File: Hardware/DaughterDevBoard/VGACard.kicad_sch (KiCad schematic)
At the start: 42 parts, among them J13 BANKA, J14 BANKB, J15 BANKD, J16 BANKC, J17 VGA_OUT, J19 BANK_A, J20 BANK_C, J21 BANK_B, J22 BANK_D, J8 PROG, Q1 2N2222A, U3 SN74LVC2T45QDCURQ1, U4 SN74LVC2T45QDCURQ1, U5 NE555P, U6 SN74LVC8T245DBQR, U7 SN74LVC8T245DBQR, U8 SN74LVC8T245DBQR, U9 SN74LVC1T45DCK

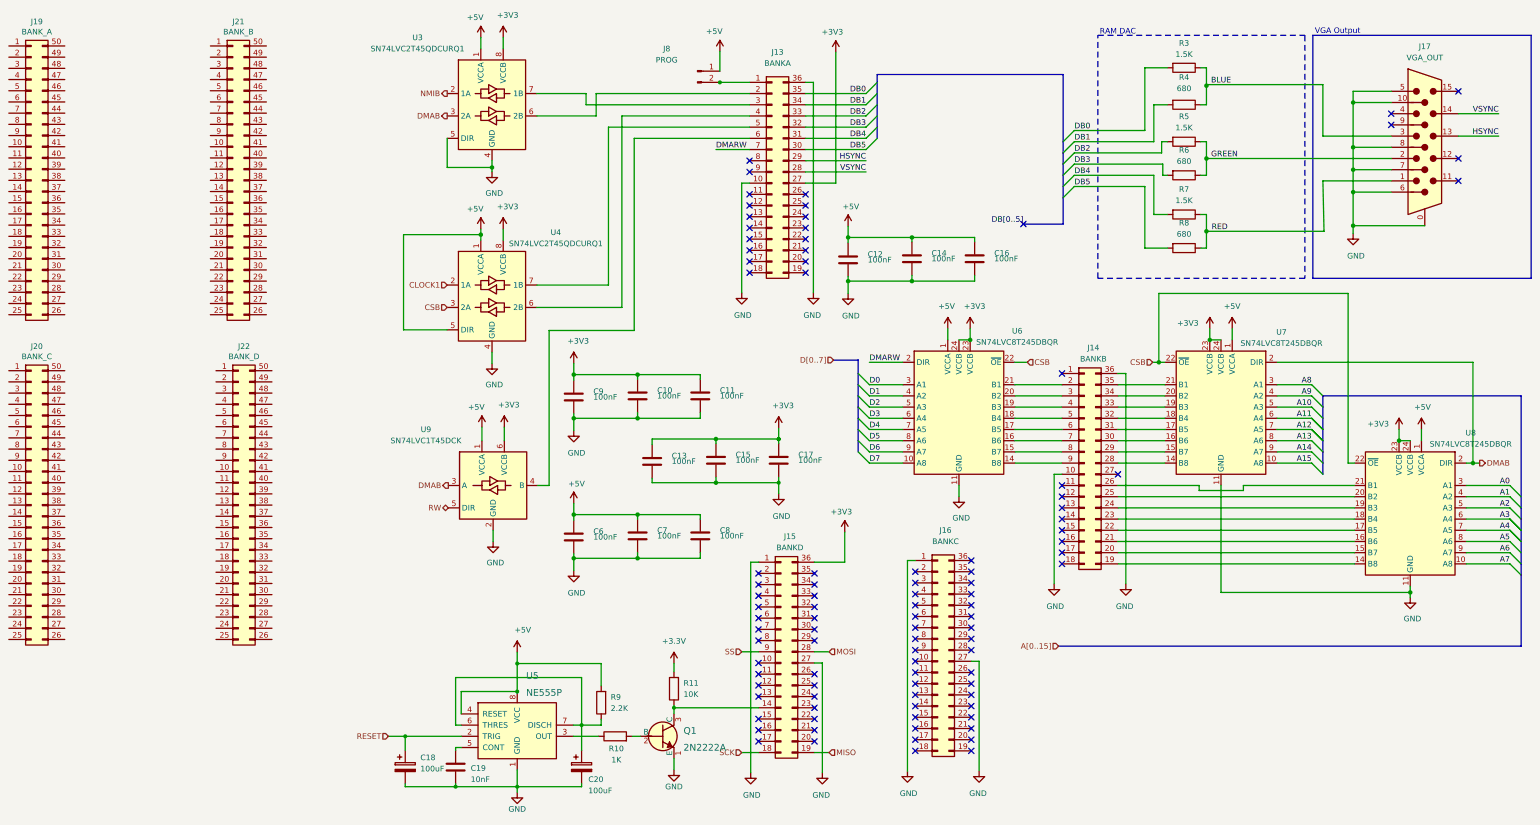
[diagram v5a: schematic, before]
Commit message: Remove Alchitry shield
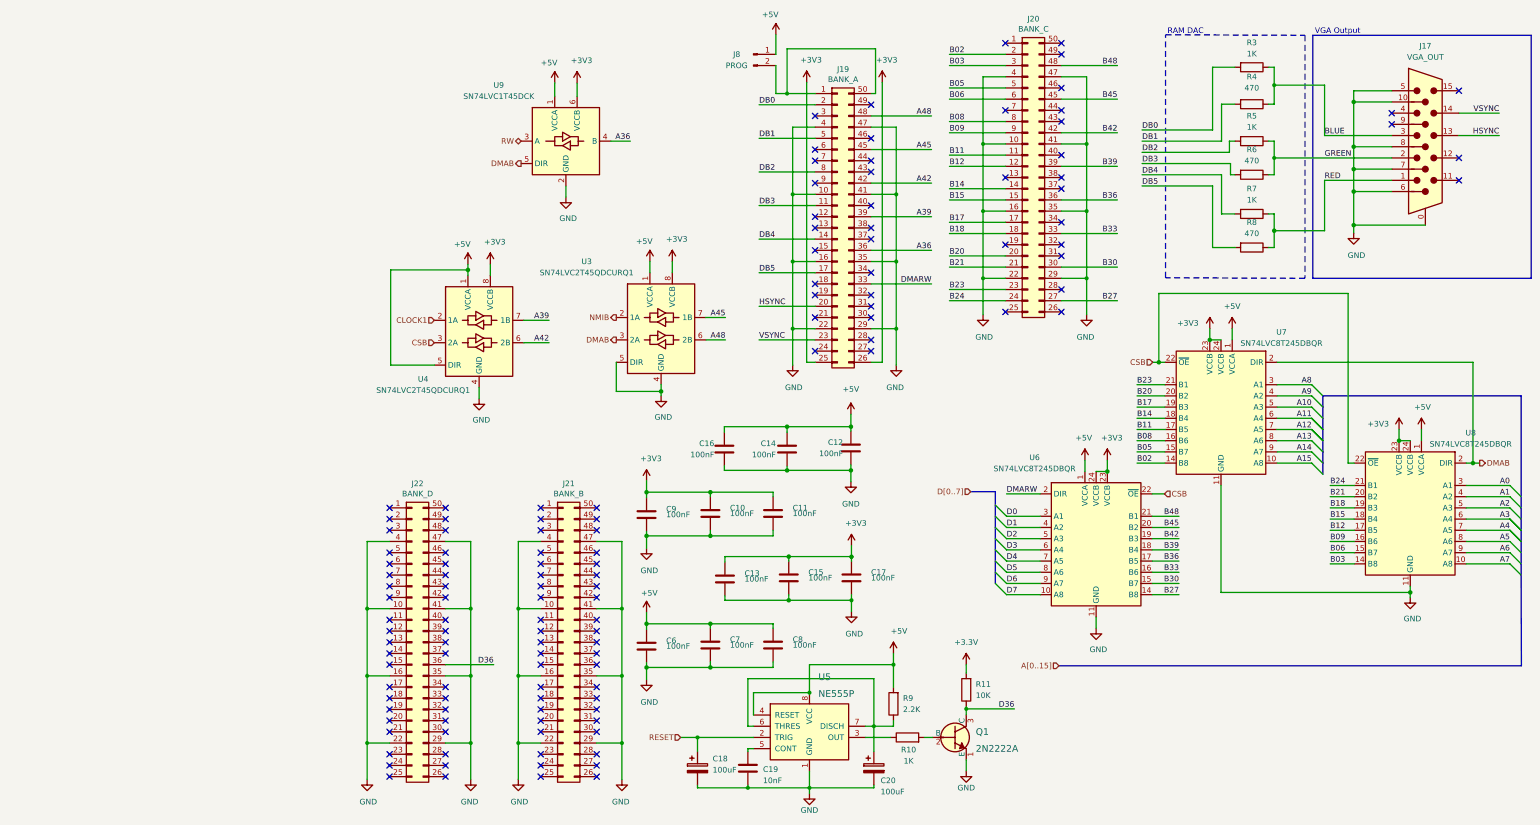
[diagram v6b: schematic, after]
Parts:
- removed J13: BANKA, Connector_TheRLab:Alchitry_Bank, symbol Connector_Generic:Conn_02x18_Counter_Clockwise
- removed J14: BANKB, Connector_TheRLab:Alchitry_Bank, symbol Connector_Generic:Conn_02x18_Counter_Clockwise
- removed J15: BANKD, Connector_TheRLab:Alchitry_Bank, symbol Connector_Generic:Conn_02x18_Counter_Clockwise
- removed J16: BANKC, Connector_TheRLab:Alchitry_Bank, symbol Connector_Generic:Conn_02x18_Counter_Clockwise
- J20: renamed from J21; value BANK_B -> BANK_C
- J21: renamed from J20; value BANK_C -> BANK_B
- R3, R5, R7: value 1.5K -> 1K
- R4, R6, R8: value 680 -> 470
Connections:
- net +3V3: now also J19.25 (Pin_25), J19.26 (Pin_26)
- net +5V: now also C12.2, C14.2, C16.2; no longer C12.1, C14.1, C16.1
- net DB0: now also J19.2 (Pin_2)
- net DB1: now also J19.5 (Pin_5)
- net DB2: now also J19.8 (Pin_8)
- net DB3: now also J19.11 (Pin_11)
- net DB4: now also J19.14 (Pin_14)
- net DB5: now also J19.17 (Pin_17)
- net DMAB: now also U9.5 (DIR); no longer U9.3 (A)
- net DMARW: now also J19.33 (Pin_33)
- net GND: now also C12.1, C14.1, C16.1, J19.10 (Pin_10), J19.16 (Pin_16), J19.22 (Pin_22), J19.29 (Pin_29), J19.35 (Pin_35), J19.4 (Pin_4), J19.41 (Pin_41), J19.47 (Pin_47), J20.10 (Pin_10), J20.16 (Pin_16), J20.22 (Pin_22), J20.29 (Pin_29), J20.35 (Pin_35), J20.4 (Pin_4), J20.41 (Pin_41), J20.47 (Pin_47), J21.10 (Pin_10), J21.16 (Pin_16), J21.22 (Pin_22), J21.29 (Pin_29), J21.35 (Pin_35), J21.4 (Pin_4), J21.41 (Pin_41), J21.47 (Pin_47), J22.10 (Pin_10), J22.16 (Pin_16), J22.22 (Pin_22), J22.29 (Pin_29), J22.35 (Pin_35), J22.4 (Pin_4), J22.41 (Pin_41), J22.47 (Pin_47); no longer C12.2, C14.2, C16.2
- net HSYNC: now also J19.20 (Pin_20)
- net RW: now also U9.3 (A); no longer U9.5 (DIR)
- net VSYNC: now also J19.23 (Pin_23)
- net D36: now reaches Q1.3 (C), R11.1
- net D36: now also J22.36 (Pin_36)
- net B03: now reaches U8.14 (B8)
- net B03: now also J20.3 (Pin_3)
- net B06: now reaches U8.15 (B7)
- net B06: now also J20.6 (Pin_6)
- net B09: now reaches U8.16 (B6)
- net B09: now also J20.9 (Pin_9)
- net B12: now reaches U8.17 (B5)
- net B12: now also J20.12 (Pin_12)
- net B15: now reaches U8.18 (B4)
- net B15: now also J20.15 (Pin_15)
- net B18: now reaches U8.19 (B3)
- net B18: now also J20.18 (Pin_18)
- net B21: now reaches U8.20 (B2)
- net B21: now also J20.21 (Pin_21)
- net B24: now reaches U8.21 (B1)
- net B24: now also J20.24 (Pin_24)
- net B11: now reaches J20.11 (Pin_11)
- net B11: now also U7.17 (B5)
- net B14: now reaches J20.14 (Pin_14)
- net B14: now also U7.18 (B4)
- net B17: now reaches J20.17 (Pin_17)
- net B17: now also U7.19 (B3)
- net B02: now reaches J20.2 (Pin_2)
- net B02: now also U7.14 (B8)
- net B20: now reaches J20.20 (Pin_20)
- net B20: now also U7.20 (B2)
- net B23: now reaches J20.23 (Pin_23)
- net B23: now also U7.21 (B1)
- net B27: now reaches J20.27 (Pin_27)
- net B27: now also U6.14 (B8)
- net B30: now reaches J20.30 (Pin_30)
- net B30: now also U6.15 (B7)
- net B33: now reaches J20.33 (Pin_33)
- net B33: now also U6.16 (B6)
- net B36: now reaches J20.36 (Pin_36)
- net B36: now also U6.17 (B5)
- net B39: now reaches J20.39 (Pin_39)
- net B39: now also U6.18 (B4)
- net B42: now reaches J20.42 (Pin_42)
- net B42: now also U6.19 (B3)
- net B45: now reaches J20.45 (Pin_45)
- net B45: now also U6.20 (B2)
- net B48: now reaches J20.48 (Pin_48)
- net B48: now also U6.21 (B1)
- net B05: now reaches J20.5 (Pin_5)
- net B05: now also U7.15 (B7)
- net B08: now reaches J20.8 (Pin_8)
- net B08: now also U7.16 (B6)
- net at J19.1 (Pin_1): now also J19.50 (Pin_50), J8.2 (Pin_2)
- net A36: now reaches J19.36 (Pin_36)
- net A36: now also U9.4 (B)
- net A39: now reaches J19.39 (Pin_39)
- net A39: now also U4.7 (1B)
- net A42: now reaches J19.42 (Pin_42)
- net A42: now also U4.6 (2B)
- net A45: now reaches J19.45 (Pin_45)
- net A45: now also U3.7 (1B)
- net A48: now reaches J19.48 (Pin_48)
- net A48: now also U3.6 (2B)
- no-connect marks 96 -> 130
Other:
- moved on the sheet: C10, C11, C12, C13, C14, C15, C16, C17, C18, C19, C20, C6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
